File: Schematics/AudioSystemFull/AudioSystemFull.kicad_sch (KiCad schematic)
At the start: 283 parts, among them IC1 TDA1558Q, J1 SJ1-3515-SMT-TR-BE, J2 DISPLAY, J3 ISO_Conn_Unit_B, J4 ISO_Conn_Unit_A, J5 Conn_02x03_Odd_Even, U1 LP3856ES-5.0, U10 LT3015EQ-5PBF, U11 OPA2134, U12 OPA2134, U13 OPA2134, U14 OPA2134, U15 OPA2134, U16 OPA2134, U17 OPA2134, U18 OPA2134, U19 OPA2134, U2 DEVKIT_V1_ESP32-WROOM-32, U20 OPA2134, U21 OPA2134, U22 OPA2134, U23 OPA2134, U24 OPA2134, U25 OPA2134, U26 OPA2134, U27 OPA2134, U3 PCM5102A, U4 OPA2134, U5 LP5907MFX-3.3, U6 LMR51420XFDDCR, U7 LMR51420YFDDCR, U8 LP5907MFX-3.3, U9 LMR51430YFDDCR

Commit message: added capacitor footprints and all known elements serial numbers
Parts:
- removed C28, C37: 1000u, symbol Device:C_Small
- added C109, C110: 100n, Capacitor_SMD:C_1206_3216Metric_Pad1.33x1.80mm_HandSolder, symbol Device:C_Small
- added C111, C28, C37: 1000u, Capacitor_THT:CP_Radial_D12.5mm_P5.00mm, symbol Device:C_Polarized_Small_US
- added U28: OPA2134, AudioSystemFootprintLibrary:OPA2134UA, symbol Amplifier_Operational:OPA2134
- C1, C2: value 2.2u -> 330n; footprint (none) -> Capacitor_SMD:C_1206_3216Metric_Pad1.33x1.80mm_HandSolder; MANUFACTURER_PART_NUMBER (none) -> GRM31C5C1E334JE01L
- C10, C101, C102, C103, C104, C105, C106, C107, C108, C15, C16, C25, C30, C31, C33, C39, C44, C45, C47, C5, C6, C61, C62, C63, C64, C65, C66, C67, C68, C69, C70, C71, C72, C73, C74, C75, C76, C77, C78, C79, C8, C80, C85, C86, C87, C88, C93, C94, C95, C96: footprint (none) -> Capacitor_SMD:C_1206_3216Metric_Pad1.33x1.80mm_HandSolder; MANUFACTURER_PART_NUMBER (none) -> VJ1206Y104JXAAR
- C100, C43, C50, C51, C52, C53, C54, C55, C56, C57, C58, C59, C60, C81, C82, C83, C84, C89, C90, C91, C92, C97, C98, C99: footprint (none) -> Capacitor_SMD:C_1206_3216Metric_Pad1.33x1.80mm_HandSolder; MANUFACTURER_PART_NUMBER (none) -> CGA5C2NP01H223J060AA
- C11, C12, C20, C3, C34, C35, C4: footprint (none) -> AudioSystemFootprintLibrary:UCZ1J100MCL1GS; MANUFACTURER_PART_NUMBER (none) -> UCZ1J100MCL1GS
- C13, C14: footprint (none) -> Capacitor_SMD:C_1206_3216Metric_Pad1.33x1.80mm_HandSolder; MANUFACTURER_PART_NUMBER (none) -> AC1206JRNPO9BN222
- C17, C29: footprint (none) -> Capacitor_SMD:C_1206_3216Metric_Pad1.33x1.80mm_HandSolder; MANUFACTURER_PART_NUMBER (none) -> C1206C103J1RACTU
- C18, C19, C22, C27: footprint (none) -> Capacitor_SMD:C_1206_3216Metric_Pad1.33x1.80mm_HandSolder; MANUFACTURER_PART_NUMBER (none) -> C1206C105K3RAC7800
- C21, C36, C40, C41, C42: footprint (none) -> Capacitor_SMD:C_1206_3216Metric_Pad1.33x1.80mm_HandSolder; MANUFACTURER_PART_NUMBER (none) -> MCASU32MAB7106KPNA01
- C23, C24: footprint (none) -> Capacitor_SMD:C_1206_3216Metric_Pad1.33x1.80mm_HandSolder; MANUFACTURER_PART_NUMBER (none) -> GRM31C5C1H224JE02L
- C26: footprint (none) -> Capacitor_THT:CP_Radial_D12.5mm_P5.00mm; MANUFACTURER_PART_NUMBER (none) -> EGPD350ELL222MK30H
- C32, C38, C46, C7, C9: footprint (none) -> Capacitor_SMD:C_1206_3216Metric_Pad1.33x1.80mm_HandSolder; MANUFACTURER_PART_NUMBER (none) -> GCJ31CR71H225KA12L
- C48, C49: footprint (none) -> Capacitor_SMD:C_1210_3225Metric_Pad1.33x2.70mm_HandSolder; MANUFACTURER_PART_NUMBER (none) -> CL32B226KAJNNNE
- IC1: MANUFACTURER_PART_NUMBER (none) -> TDA1558Q
- J1: MANUFACTURER_PART_NUMBER (none) -> SJ1-3515-SMT-TR-BE
- R1, R3: MANUFACTURER_PART_NUMBER (none) -> RT1206DRE0710KL
- R10, R15, R45: MANUFACTURER_PART_NUMBER (none) -> RNCU1206BTE100K
- R100, R101, R102, R55, R56, R57, R58, R99: MANUFACTURER_PART_NUMBER (none) -> RT1206FRE077K5L
- R103, R104, R105, R106, R107, R108, R109, R11, R110, R115, R116, R117, R118, R119, R12, R120, R123, R124, R125, R126, R127, R128, R13, R14, R17, R18, R21, R23, R31, R33, R41, R48, R51, R53, R59, R60, R61, R62, R63, R64, R65, R66, R69, R70, R79, R80, R90, R92, R95, R96: MANUFACTURER_PART_NUMBER (none) -> RNCP1206FTD1K00
- R111, R112, R5, R6: MANUFACTURER_PART_NUMBER (none) -> RT1206DRE07470RL
- R113, R114, R121, R122, R16, R20, R29, R30, R49, R50, R67, R68, R77, R78, R93, R94: MANUFACTURER_PART_NUMBER (none) -> RT1206BRD075KL
- R19: MANUFACTURER_PART_NUMBER (none) -> HRG3216P-1800-D-T1
- R2: MANUFACTURER_PART_NUMBER (none) -> HRG3216P-2400-D-T1
- R22, R24, R32, R34, R52, R54, R71, R72, R81, R82, R97, R98: MANUFACTURER_PART_NUMBER (none) -> RN73R2ATTD5000B25
- R25, R26, R27, R28, R73, R74, R75, R76: MANUFACTURER_PART_NUMBER (none) -> RT1206FRE0716KL
- R35, R37, R38, R42, R83, R84, R85, R86: MANUFACTURER_PART_NUMBER (none) -> RT1206DRE0712KL
- R36, R43, R87, R88: MANUFACTURER_PART_NUMBER (none) -> RT1206DRE0756KL
- R39, R47, R89, R91: MANUFACTURER_PART_NUMBER (none) -> RT1206FRD072KL
- R4: MANUFACTURER_PART_NUMBER (none) -> HRG3216P-1102-D-T1
- R40, R44: MANUFACTURER_PART_NUMBER (none) -> RN732BTTD3200F50
- R46: MANUFACTURER_PART_NUMBER (none) -> HRG3216P-1202-D-T1
- R7: MANUFACTURER_PART_NUMBER (none) -> HRG3216P-2701-D-T1
- R8, R9: MANUFACTURER_PART_NUMBER (none) -> RNCU1206BTE10K0
- RV1, RV2, RV3, RV4, RV5, RV6, RV7, RV8: MANUFACTURER_PART_NUMBER (none) -> PTN092H10120K1B
- U1: MANUFACTURER_PART_NUMBER (none) -> LP3856ES-5.0
- U10: MANUFACTURER_PART_NUMBER lt3015eq5#pbf -> LT3015EQ-5PBF
- U11, U12, U13, U14, U15, U16, U17, U18, U19, U20, U21, U22, U23, U24, U25, U26, U27, U4: MANUFACTURER_PART_NUMBER (none) -> OPA2134UA
- U2: MANUFACTURER_PART_NUMBER (none) -> MODULE_DEVKIT_V1_ESP32-WROOM-32
- U3: MANUFACTURER_PART_NUMBER (none) -> PCM5102A
- U5, U8: MANUFACTURER_PART_NUMBER (none) -> LP5907MFX-3.3
- U6: MANUFACTURER_PART_NUMBER (none) -> LMR51420XFDDCR
- U7: MANUFACTURER_PART_NUMBER (none) -> LMR51420YFDDCR
- U9: MANUFACTURER_PART_NUMBER (none) -> LMR51430YFDDCR
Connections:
- net +12VPerm: now also C111.1, C28.1, C37.1
- net +5VAnalog: now also C109.1, U28.8 (V+)
- net -5VAnalog: now also C110.1, U28.4 (V-)
- net GNDA: now also C109.2, C110.2, C111.2, C28.2, C37.2
- net at C2.2: now also U28.5 (+); no longer R40.1
- net at C1.2: now also U28.3 (+); no longer R44.1
- new net: R44.1, U28.1, U28.2 (-)
- new net: R40.1, U28.6 (-), U28.7

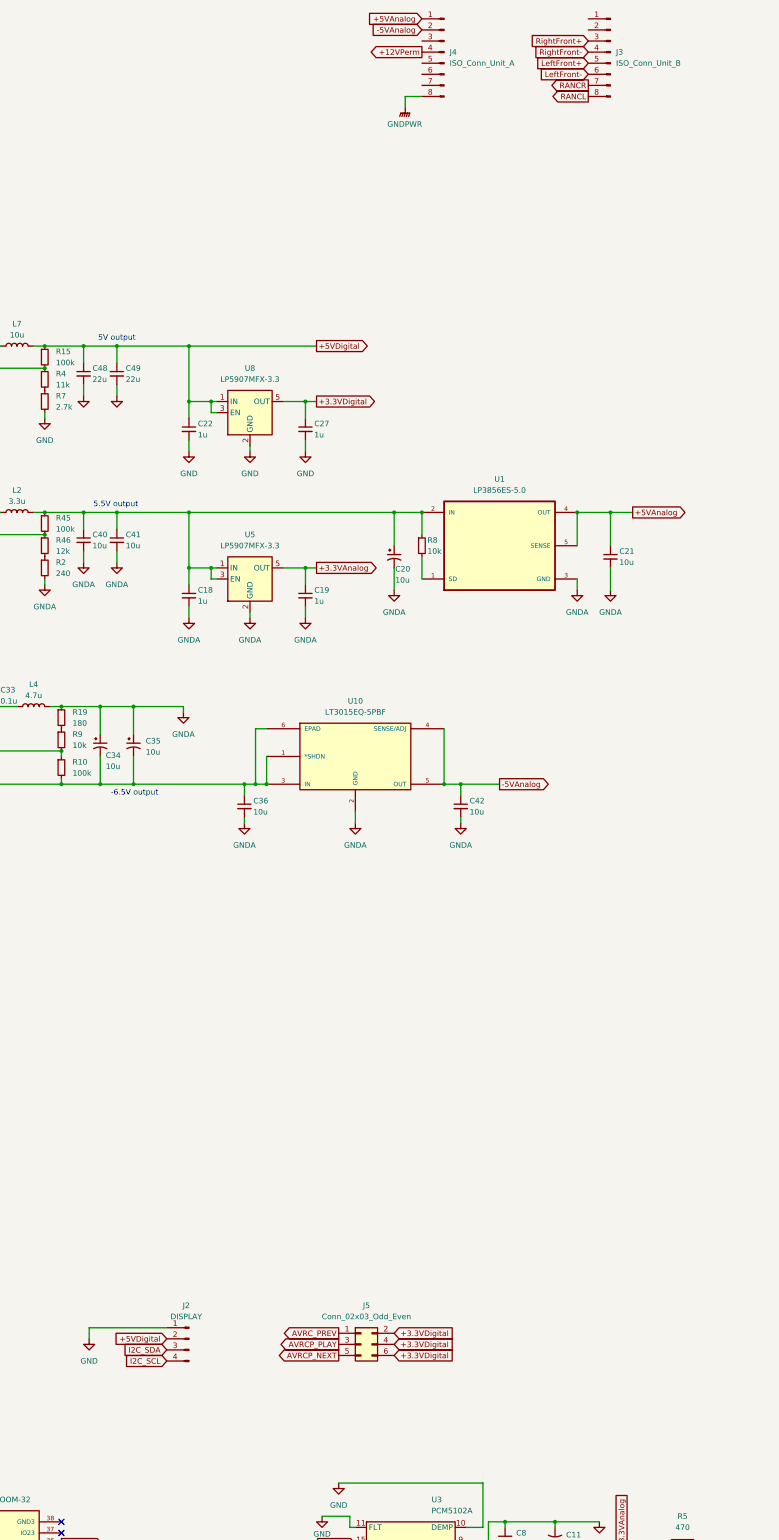
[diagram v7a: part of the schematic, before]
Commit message: added all footprints
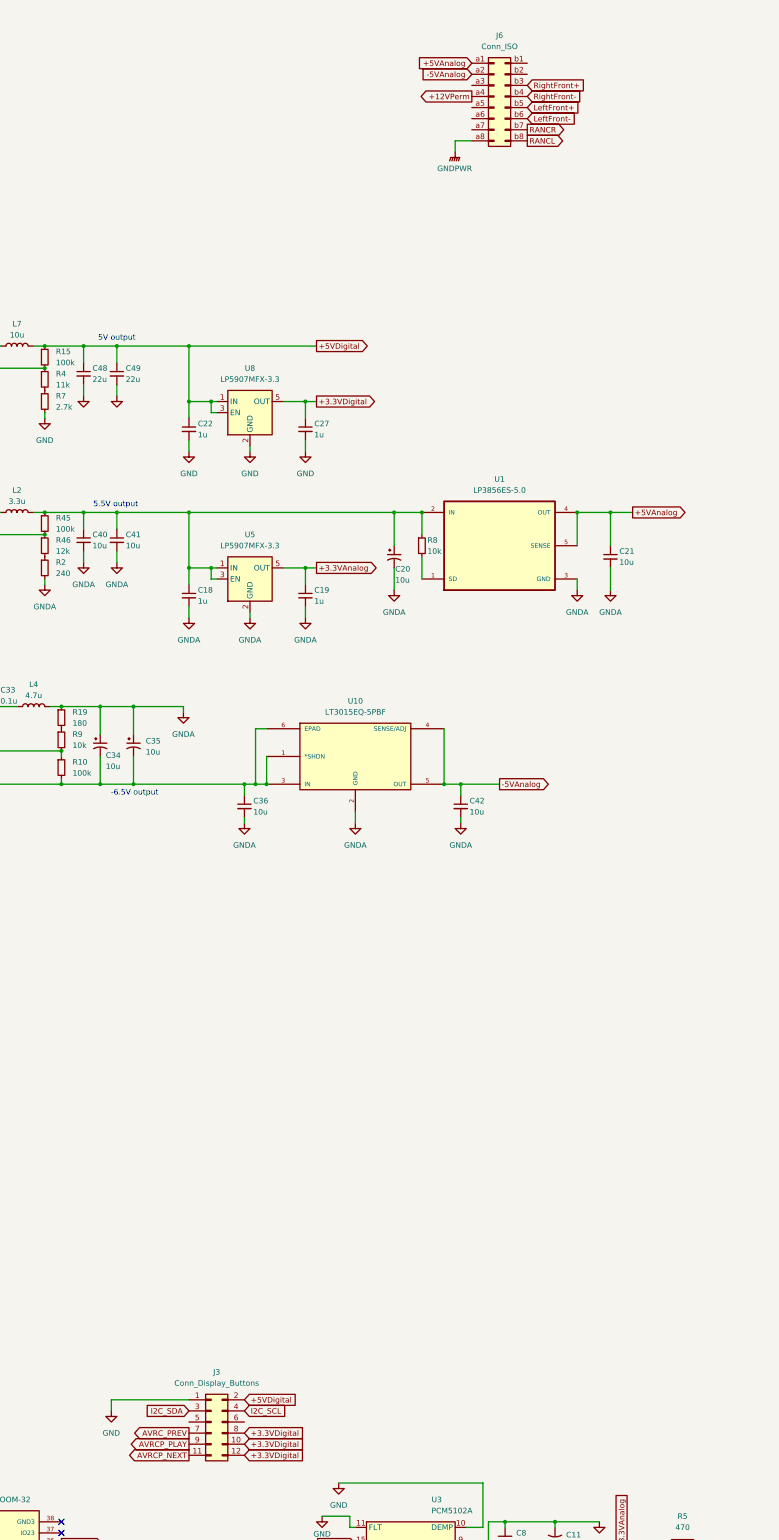
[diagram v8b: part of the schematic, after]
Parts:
- removed J2: DISPLAY, symbol Connector:Conn_01x04_Pin
- removed J3: ISO_Conn_Unit_B, symbol Connector:Conn_01x08_Pin
- removed J4: ISO_Conn_Unit_A, symbol Connector:Conn_01x08_Pin
- removed J5: Conn_02x03_Odd_Even, symbol Connector_Generic:Conn_02x03_Odd_Even
- added J3: Conn_Display_Buttons, AudioSystemFootprintLibrary:Molex-43045-1211, symbol Connector_Generic:Conn_02x06_Odd_Even
- added J6: Conn_ISO, AudioSystemFootprintLibrary:Conn_ISO_Solder_Pad, symbol Connector_Generic:Conn_02x08_Row_Letter_First
- L1, L3, L6: footprint (none) -> AudioSystemFootprintLibrary:SRP0315-1R0K; MANUFACTURER_PART_NUMBER (none) -> SRP0315-1R0K
- L2: footprint (none) -> AudioSystemFootprintLibrary:SRP5030T-3R3M; MANUFACTURER_PART_NUMBER (none) -> SRP5030T-3R3M
- L4: footprint (none) -> AudioSystemFootprintLibrary:VLS6045EX-4R7M-H; MANUFACTURER_PART_NUMBER (none) -> VLS6045EX-4R7M-H
- L7: footprint (none) -> AudioSystemFootprintLibrary:SRR1280A-100M; MANUFACTURER_PART_NUMBER (none) -> SRR1280A-100M
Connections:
- net +12VPerm: now also J6.a4 (Pin_a4)
- net +3.3VDigital: now also J3.10 (Pin_10), J3.12 (Pin_12), J3.8 (Pin_8)
- net +5VAnalog: now also J6.a1 (Pin_a1)
- net +5VDigital: now also J3.2 (Pin_2)
- net -5VAnalog: now also J6.a2 (Pin_a2)
- net AVRCP_NEXT: now also J3.11 (Pin_11)
- net AVRCP_PLAY: now also J3.9 (Pin_9)
- net AVRC_PREV: now also J3.7 (Pin_7)
- net GND: now also J3.1 (Pin_1)
- net GNDPWR: now also J6.a8 (Pin_a8)
- net I2C_SCL: now also J3.4 (Pin_4)
- net I2C_SDA: now also J3.3 (Pin_3)
- net LeftFront+: now also J6.b5 (Pin_b5)
- net LeftFront-: now also J6.b6 (Pin_b6)
- net RANCL: now also J6.b8 (Pin_b8)
- net RANCR: now also J6.b7 (Pin_b7)
- net RightFront+: now also J6.b3 (Pin_b3)
- net RightFront-: now also J6.b4 (Pin_b4)
